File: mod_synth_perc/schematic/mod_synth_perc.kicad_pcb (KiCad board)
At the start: 2 copper layers, 41.9 x 109.2 mm, 48 parts, among them J1 Trigger, J2 Conn_01x04_Male, J3 Conn_02x05_Odd_Even, J4 Out, J5 Conn_01x07_Male, J6 Conn_01x07_Female, J7 Conn_01x07_Male, J8 Conn_01x07_Female, Q1 2N3904, Q2 2N3904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

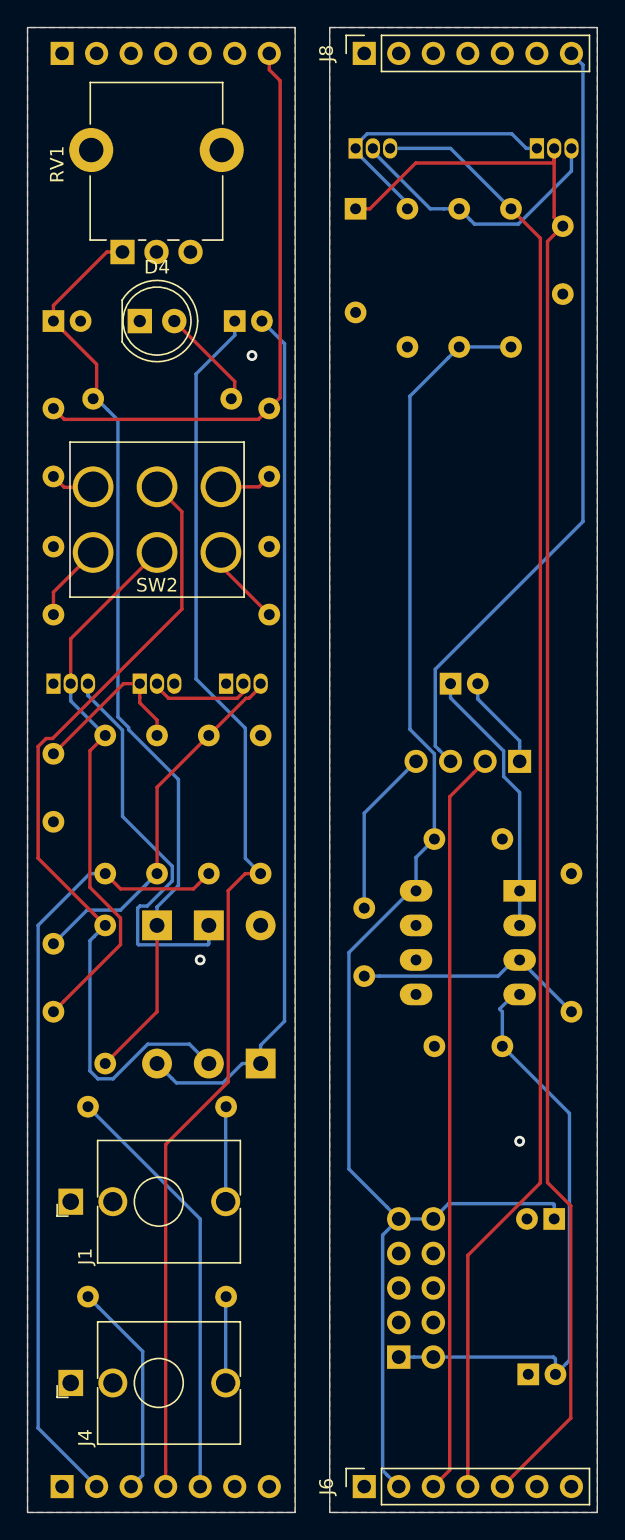
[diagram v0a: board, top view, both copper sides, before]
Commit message: Align front panel components
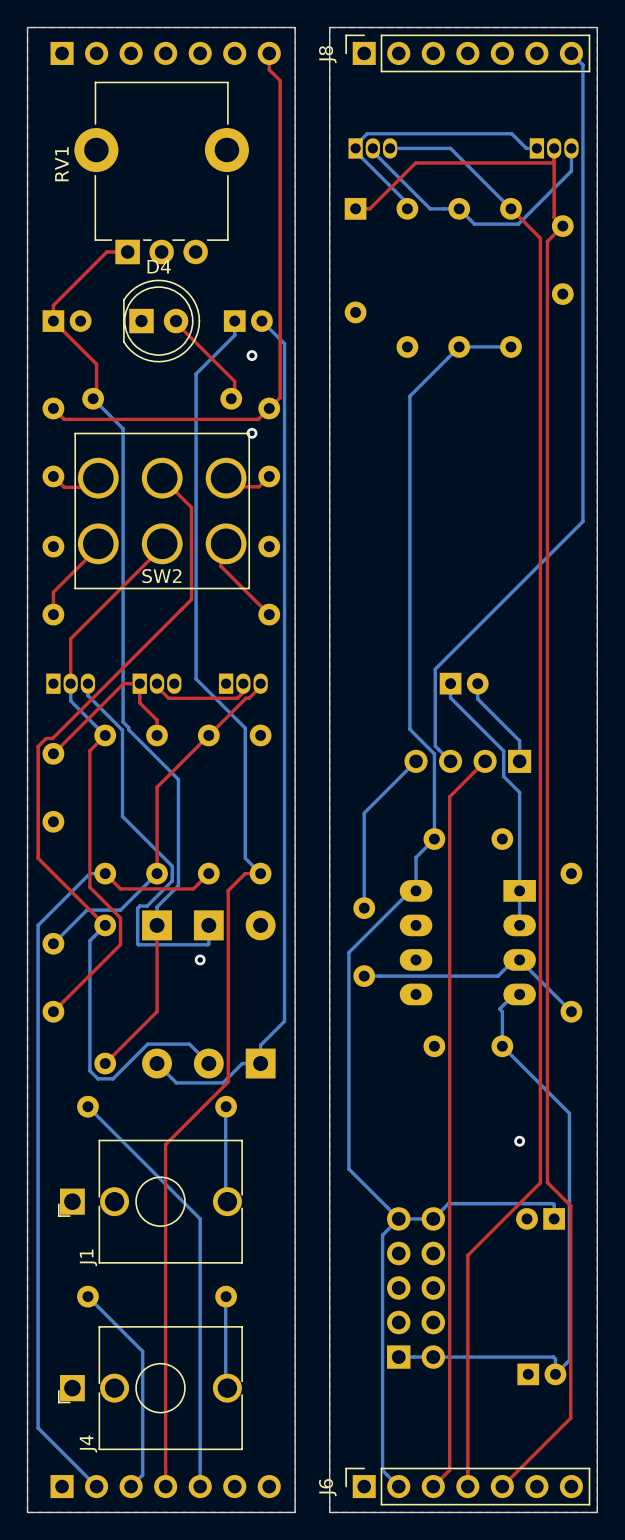
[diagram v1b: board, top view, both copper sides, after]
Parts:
- moved SW2 0.74 mm to (41.7, 86.4)
- moved J4 0.40 mm to (35.1, 150.9)
- moved RV1 0.38 mm to (39.1, 67.3)
- moved J1 0.13 mm to (35.1, 137.2)
- moved D4 0.13 mm to (40.1, 72.4)
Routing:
- net /C2_IN: track 61.5 -> 62.8 mm
- net /GND_PCB_B: vias 2 -> 3
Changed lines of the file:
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@@
     (thickness 1.6)
     (drawings 8)
-    (tracks 236)
+    (tracks 238)
     (zones 0)
     (modules 48)
@@
     (solder_mask_min_width 0.25)
     (aux_axis_origin 0 0)
-    (visible_elements FFFFFF7F)
+    (visible_elements 7FFFFFFF)
     (pcbplotparams
       (layerselection 0x010fc_ffffffff)
@@
   )
   (module mod_synth:DPDT_Switch_Vertical (layer F.Cu)
-    (at 41.275 86.995)
+    (at 41.656 86.36)
     (fp_text reference SW2 (at 0 4.826) (layer F.SilkS)
       (effects (font (size 1 1) (thickness 0.15)))
@@
   )
   (module Potentiometer_THT:Potentiometer_Alpha_RD901F-40-00D_Single_Vertical_CircularHoles (layer F.Cu)
-    (at 38.735 67.31 90)
+    (at 39.116 67.31 90)
     (descr "Potentiometer, vertical, 9mm, single, http://www.taiwanalpha.com.tw/downloads?target=products&id=113")
     (tags "potentiometer vertical 9mm single")
@@
   )
   (module Connector_Audio:Jack_3.5mm_QingPu_WQP-PJ398SM_Vertical_CircularHoles (layer F.Cu)
-    (at 34.925 150.495 90)
+    (at 35.052 150.876 90)
     (descr "TRS 3.5mm, vertical, Thonkiconn, PCB mount, (http://www.qingpu-electronics.com/en/products/WQP-PJ398SM-362.html)")
     (tags "WQP-PJ398SM WQP-PJ301M-12 TRS 3.5mm mono vertical jack thonkiconn qingpu")
@@
   )
   (module Connector_Audio:Jack_3.5mm_QingPu_WQP-PJ398SM_Vertical_CircularHoles (layer F.Cu)
-    (at 34.925 137.16 90)
+    (at 35.052 137.16 90)
     (descr "TRS 3.5mm, vertical, Thonkiconn, PCB mount, (http://www.qingpu-electronics.com/en/products/WQP-PJ398SM-362.html)")
     (tags "WQP-PJ398SM WQP-PJ301M-12 TRS 3.5mm mono vertical jack thonkiconn qingpu")
@@
   )
   (module LED_THT:LED_D5.0mm (layer F.Cu)
-    (at 40.005 72.39)
+    (at 40.132 72.39)
     (descr "LED, diameter 5.0mm, 2 pins, http://cdn-reichelt.de/documents/datenblatt/A500/LL-504BC2E-009.pdf")
     (tags "LED diameter 5.0mm 2 pins")
@@
   (segment (start 41.275 116.84) (end 41.275 123.19) (width 0.25) (layer F.Cu) (net 11))
   (segment (start 41.275 115.49) (end 42.850012 113.914988) (width 0.25) (layer B.Cu) (net 11))
-  (segment (start 38.400001 101.503589) (end 38.400001 79.675001) (width 0.25) (layer B.Cu) (net 11))
   (segment (start 42.850012 106.110014) (end 39.185011 102.445013) (width 0.25) (layer B.Cu) (net 11))
   (segment (start 39.185011 102.445013) (end 39.185011 102.288598) (width 0.25) (layer B.Cu) (net 11))
-  (segment (start 37.629999 78.904999) (end 36.83 78.105) (width 0.25) (layer B.Cu) (net 11))
   (segment (start 41.275 116.84) (end 41.275 115.49) (width 0.25) (layer B.Cu) (net 11))
-  (segment (start 38.400001 79.675001) (end 37.629999 78.904999) (width 0.25) (layer B.Cu) (net 11))
   (segment (start 42.850012 113.914988) (end 42.850012 106.110014) (width 0.25) (layer B.Cu) (net 11))
-  (segment (start 39.185011 102.288598) (end 38.400001 101.503589) (width 0.25) (layer B.Cu) (net 11))
+  (segment (start 38.781001 101.884588) (end 39.185011 102.288598) (width 0.25) (layer B.Cu) (net 11))
+  (segment (start 38.781001 80.310001) (end 38.781001 101.884588) (width 0.25) (layer B.Cu) (net 11))
+  (segment (start 36.576 78.105) (end 38.781001 80.310001) (width 0.25) (layer B.Cu) (net 11))
   (segment (start 67.945 103.675) (end 67.945 104.775) (width 0.25) (layer B.Cu) (net 12))
   (segment (start 67.945 103.27137) (end 67.945 103.675) (width 0.25) (layer B.Cu) (net 12))
@@
   (segment (start 33.114999 103.094999) (end 32.529999 103.679999) (width 0.25) (layer F.Cu) (net 18))
   (segment (start 32.529999 111.904999) (end 36.665001 116.040001) (width 0.25) (layer F.Cu) (net 18))
-  (segment (start 43.100001 93.582094) (end 33.587096 103.094999) (width 0.25) (layer F.Cu) (net 18))
-  (segment (start 43.100001 86.405001) (end 43.100001 93.582094) (width 0.25) (layer F.Cu) (net 18))
   (segment (start 33.587096 103.094999) (end 33.114999 103.094999) (width 0.25) (layer F.Cu) (net 18))
-  (segment (start 41.275 84.58) (end 43.100001 86.405001) (width 0.25) (layer F.Cu) (net 18))
   (segment (start 36.339999 117.965001) (end 36.665001 117.639999) (width 0.25) (layer B.Cu) (net 18))
   (segment (start 36.339999 127.540001) (end 36.339999 117.965001) (width 0.25) (layer B.Cu) (net 18))
@@
   (segment (start 36.665001 117.639999) (end 37.465 116.84) (width 0.25) (layer B.Cu) (net 18))
   (segment (start 45.085 127) (end 43.659999 125.574999) (width 0.25) (layer B.Cu) (net 18))
+  (segment (start 43.815 92.867096) (end 42.941048 93.741048) (width 0.25) (layer F.Cu) (net 18))
+  (segment (start 43.815 86.104) (end 43.815 92.867096) (width 0.25) (layer F.Cu) (net 18))
+  (segment (start 41.656 83.945) (end 43.815 86.104) (width 0.25) (layer F.Cu) (net 18))
+  (segment (start 43.100001 93.582094) (end 42.941048 93.741048) (width 0.25) (layer F.Cu) (net 18))
+  (segment (start 42.941048 93.741048) (end 33.587096 103.094999) (width 0.25) (layer F.Cu) (net 18))
   (segment (start 45.085 118.19) (end 45.085 116.84) (width 0.25) (layer B.Cu) (net 19))
   (segment (start 39.914999 118.265001) (end 45.009999 118.265001) (width 0.25) (layer B.Cu) (net 19))
@@
   (segment (start 46.325 130.205) (end 46.355 130.175) (width 0.25) (layer B.Cu) (net 20))
   (segment (start 46.325 137.16) (end 46.325 130.205) (width 0.25) (layer B.Cu) (net 20))
-  (segment (start 64.555001 105.624999) (end 65.405 104.775) (width 0.25) (layer F.Cu) (net 54))
-  (segment (start 62.800001 107.379999) (end 64.555001 105.624999) (width 0.25) (layer F.Cu) (net 54))
-  (segment (start 62.800001 156.909999) (end 62.800001 107.379999) (width 0.25) (layer F.Cu) (net 54))
-  (segment (start 61.595 158.115) (end 62.800001 156.909999) (width 0.25) (layer F.Cu) (net 54))
   (segment (start 46.325 144.175) (end 46.355 144.145) (width 0.25) (layer B.Cu) (net 21))
   (segment (start 46.325 150.495) (end 46.325 144.175) (width 0.25) (layer B.Cu) (net 21))
@@
   (segment (start 41.275 99.06) (end 41.275 99.285) (width 0.25) (layer F.Cu) (net 24))
   (segment (start 47.625 99.693589) (end 47.625 99.06) (width 0.25) (layer F.Cu) (net 24))
+  (via (at 44.45 119.38) (size 0.8) (drill 0.4) (layers F.Cu B.Cu) (net 29))
   (via (at 48.26 74.93) (size 0.8) (drill 0.4) (layers F.Cu B.Cu) (net 29))
-  (via (at 44.45 119.38) (size 0.8) (drill 0.4) (layers F.Cu B.Cu) (net 29))
+  (via (at 48.26 80.645) (size 0.8) (drill 0.4) (layers F.Cu B.Cu) (net 29))
   (segment (start 36.33363 113.03) (end 37.465 113.03) (width 0.25) (layer B.Cu) (net 30))
   (segment (start 32.529999 116.833631) (end 36.33363 113.03) (width 0.25) (layer B.Cu) (net 30))
@@
   (segment (start 71.755 52.705) (end 72.60501 53.55501) (width 0.25) (layer B.Cu) (net 53))
   (segment (start 62.015001 103.925001) (end 62.865 104.775) (width 0.25) (layer B.Cu) (net 53))
+  (segment (start 64.555001 105.624999) (end 65.405 104.775) (width 0.25) (layer F.Cu) (net 54))
+  (segment (start 62.800001 107.379999) (end 64.555001 105.624999) (width 0.25) (layer F.Cu) (net 54))
+  (segment (start 62.800001 156.909999) (end 62.800001 107.379999) (width 0.25) (layer F.Cu) (net 54))
+  (segment (start 61.595 158.115) (end 62.800001 156.909999) (width 0.25) (layer F.Cu) (net 54))
   (zone (net 1) (net_name GND) (layer F.Cu) (hatch edge 0.508)
     (connect_pads (clearance 0.508))
